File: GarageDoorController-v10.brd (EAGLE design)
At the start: 81 x 45.2 mm, 21 parts, among them IC1 ATMEGA328, IC2 TO-220, J1 ICSP, J2 DCJ0202, Q1 2N2222A, X1 Garage Door, X2 Reed Switch, X3 ETH SHLD, X4 ETH SHLD, Y1 16MHz

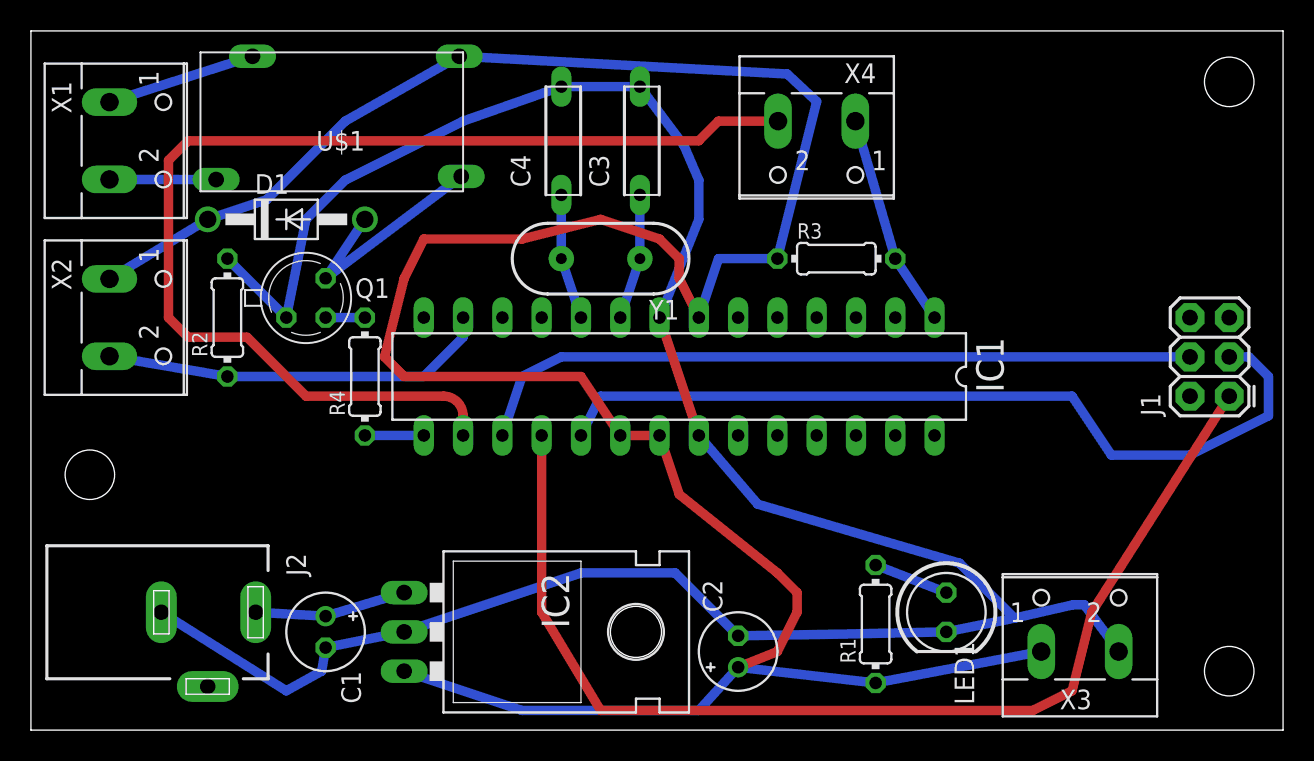
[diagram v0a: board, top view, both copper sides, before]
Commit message: Updated 'GarageDoorController-v10.brd':
Fixed the 'short' in the trace near the top of the board.
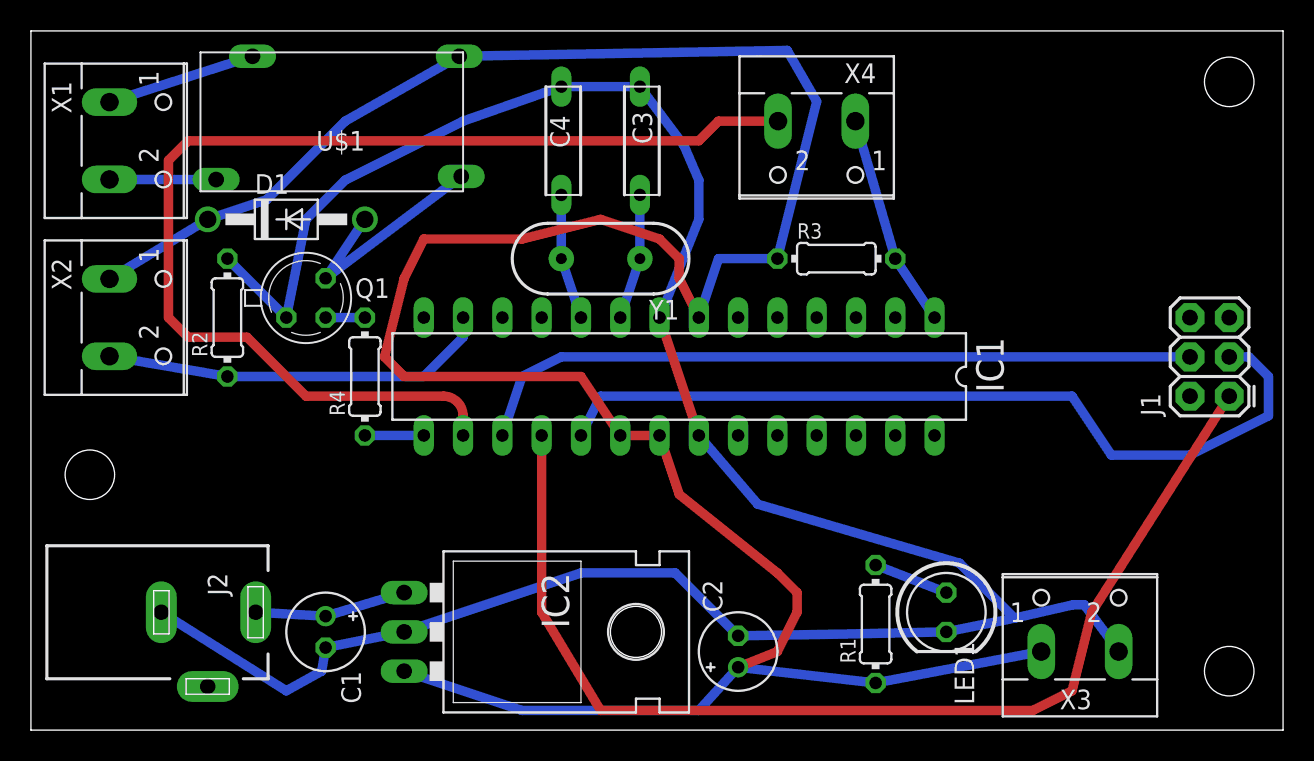
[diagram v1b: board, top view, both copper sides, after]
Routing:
- net +5V: track 183.1 -> 184.2 mm
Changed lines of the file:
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@@
 <attribute name="MF" value="" x="-33.02" y="-7.62" size="1.778" layer="27" rot="R270" display="off"/>
 <attribute name="OC_FARNELL" value="unknown" x="-33.02" y="-7.62" size="1.778" layer="27" rot="R270" display="off"/>
-<attribute name="VALUE" x="3.81" y="31.71" size="1.27" layer="27" ratio="10"/>
+<attribute name="VALUE" x="1.27" y="38.06" size="1.27" layer="27" ratio="10"/>
 <attribute name="NAME" x="1.3462" y="41.9462" size="1.27" layer="25" ratio="10" rot="R270"/>
 </element>
@@
 <attribute name="NAME" x="1.3462" y="30.5162" size="1.27" layer="25" ratio="10" rot="R270"/>
 </element>
-<element name="Y1" library="SparkFun-FreqCtrl" package="HC49US" value="16MHz" x="36.83" y="30.48" rot="R180"/>
+<element name="Y1" library="SparkFun-FreqCtrl" package="HC49US" value="16MHz" x="36.83" y="30.48" smashed="yes" rot="R180">
+<attribute name="VALUE" x="39.878" y="29.591" size="1.27" layer="27" ratio="10" rot="R180"/>
+<attribute name="NAME" x="41.91" y="27.813" size="1.27" layer="25" ratio="10" rot="R180"/>
+</element>
 <element name="C1" library="rcl" package="E2-5" value="10uF" x="19.05" y="6.35" smashed="yes" rot="R270">
 <attribute name="NAME" x="20.066" y="3.81" size="1.27" layer="25" ratio="10" rot="R270"/>
@@
 <attribute name="MF" value="" x="0" y="-26.67" size="1.778" layer="27" rot="R270" display="off"/>
 <attribute name="OC_FARNELL" value="unknown" x="0" y="-26.67" size="1.778" layer="27" rot="R270" display="off"/>
-<attribute name="NAME" x="16.51" y="11.43" size="1.27" layer="25" rot="R270"/>
+<attribute name="NAME" x="11.43" y="10.16" size="1.27" layer="25" rot="R270"/>
 <attribute name="VALUE" x="1.27" y="12.7" size="1.27" layer="27"/>
 </element>
@@
 <element name="R3" library="resistor" package="0204/7" value="10K" x="52.07" y="30.48"/>
 <element name="R4" library="resistor" package="0204/7" value="1K" x="21.59" y="22.86" rot="R90"/>
-<element name="C3" library="domiflichi" package="1440PH" value="1440PH" x="39.37" y="38.1"/>
-<element name="C4" library="domiflichi" package="1440PH" value="1440PH" x="34.29" y="38.1"/>
+<element name="C3" library="domiflichi" package="1440PH" value="1440PH" x="39.37" y="38.1" smashed="yes">
+<attribute name="NAME" x="40.164" y="37.893996875" size="1.27" layer="25" rot="R90"/>
+<attribute name="VALUE" x="42.370003125" y="35.099996875" size="1.27" layer="27" rot="R90"/>
+</element>
+<element name="C4" library="domiflichi" package="1440PH" value="1440PH" x="34.29" y="38.1" smashed="yes">
+<attribute name="NAME" x="34.83" y="37.639996875" size="1.27" layer="25" rot="R90"/>
+<attribute name="VALUE" x="32.972003125" y="34.845996875" size="1.27" layer="27" rot="R90"/>
+</element>
 <element name="U$1" library="domiflichi" package="PB874" value="PB874FORMA" x="27.94" y="43.815" rot="R180"/>
 <element name="X3" library="con-wago-500" package="W237-102" value="ETH SHLD" x="67.818" y="6.35" smashed="yes">
@@
 <wire x1="15.24" y1="34.29" x2="11.43" y2="33.02" width="0.6096" layer="16"/>
 <wire x1="48.26" y1="30.48" x2="50.8" y2="40.64" width="0.6096" layer="16"/>
-<wire x1="50.8" y1="40.64" x2="48.895" y2="42.418" width="0.6096" layer="16"/>
+<wire x1="50.8" y1="40.64" x2="48.895" y2="43.942" width="0.6096" layer="16"/>
 <wire x1="5.08" y1="29.17" x2="11.43" y2="33.02" width="0.6096" layer="16"/>
 <wire x1="38.1" y1="19.05" x2="40.64" y2="19.05" width="0.6096" layer="1"/>
@@
 <wire x1="44.45" y1="30.48" x2="48.26" y2="30.48" width="0.6096" layer="16"/>
 <wire x1="27.69" y1="43.565" x2="20.32" y2="39.37" width="0.6096" layer="16"/>
-<wire x1="27.69" y1="43.565" x2="48.895" y2="42.418" width="0.6096" layer="16"/>
+<wire x1="27.69" y1="43.565" x2="48.895" y2="43.942" width="0.6096" layer="16"/>
 <wire x1="43.18" y1="26.67" x2="41.91" y2="29.21" width="0.6096" layer="1"/>
 <wire x1="41.91" y1="29.21" x2="41.91" y2="30.48" width="0.6096" layer="1"/>
